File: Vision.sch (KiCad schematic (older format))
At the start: 125 parts, among them J1 Conn_ARM_JTAG_SWD_10, Q1 DTC123J, SW1 SW_Push, U1 MCP1700-3002E_SOT23, U2 STM32F072CBUx, U3 TPD4E05U06DQAR

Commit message: Set switch position
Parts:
- K_,1, K_.1, K_;1, K_A1, K_B1, K_B2, K_C1, K_D1, K_E1, K_F1, K_G1, K_H1, K_I1, K_J1, K_K1, K_L1, K_M1, K_N1, K_O1, K_P1, K_Q1, K_R1, K_S1, K_T1, K_U1, K_V1, K_W1, K_X1, K_Y1, K_Z1: footprint MX_Only:MXOnly-1U-Hotswap-Antishear -> MX_Only:MXOnly-1U-Hotswap
- K_ALT1: value MX-1U -> MX-1.5U; footprint MX_Only:MXOnly-1U-Hotswap-Antishear -> MX_Only:MXOnly-1.5U-Hotswap
- K_ALT2, K_CTRL1, K_CTRL2: value MX-1.25U -> MX-1.5U; footprint MX_Only:MXOnly-1U-Hotswap-Antishear -> MX_Only:MXOnly-1.5U-Hotswap
- K_BSPC1: renamed from K_P2; footprint MX_Only:MXOnly-1U-Hotswap-Antishear -> MX_Only:MXOnly-1U-Hotswap
- K_DEL1, K_ESC1, K_PGUP1: value MX-1.5U -> MX-1U; footprint MX_Only:MXOnly-1U-Hotswap-Antishear -> MX_Only:MXOnly-1U-Hotswap
- K_ENTER1, K_SHIFT1: value MX-2.25U -> MX-1.75U; footprint MX_Only:MXOnly-1U-Hotswap-Antishear -> MX_Only:MXOnly-1.75U-Hotswap
- K_FN1, K_PGDN1: value MX-1.75U -> MX-1U; footprint MX_Only:MXOnly-1U-Hotswap-Antishear -> MX_Only:MXOnly-1U-Hotswap
- K_SHIFT2, K_TAB1: value MX-1.75U -> MX-1.25U; footprint MX_Only:MXOnly-1U-Hotswap-Antishear -> MX_Only:MXOnly-1.25U-Hotswap
- K_SPC1: value MX-1.25U -> MX-2U; footprint MX_Only:MXOnly-1U-Hotswap-Antishear -> MX_Only:MXOnly-2U-Hotswap-ReversedStabilizers
- K_SPC2: value MX-6U -> MX-1.75U; footprint MX_Only:MXOnly-1U-Hotswap-Antishear -> MX_Only:MXOnly-1.75U-Hotswap
- K_WIN1: value MX-2.25U -> MX-1U; footprint MX_Only:MXOnly-1U-Hotswap-Antishear -> MX_Only:MXOnly-1U-Hotswap
- K_WIN2: value MX-2.75U -> MX-1U; footprint MX_Only:MXOnly-1U-Hotswap-Antishear -> MX_Only:MXOnly-1U-Hotswap
- R1, R2, R3, R4, R5, R6: footprint Resistors_SMD:R_0805 -> Resistor_SMD:R_0603_1608Metric
- U2: symbol MCU_ST_STM32F0:STM32F072CBUx -> MCU_ST_STM32F0:STM32F072CBTx
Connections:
- net GND: no longer U2.49 (VSS)

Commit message: Route PCB
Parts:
- added C13: 100nF, Capacitor_SMD:C_0603_1608Metric, symbol Device:C_Small
- added H1: LOGO1, locallib:logo1, symbol Mechanical:MountingHole
- added H2: LOGO2, locallib:logo2, symbol Mechanical:MountingHole
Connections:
- net +3V3: now also C13.1
- net COL0: now also U2.19 (PB1); no longer U2.31 (PA10)
- net COL1: now also U2.18 (PB0); no longer U2.21 (PB10)
- net COL10: now also U2.41 (PB5); no longer U2.11 (PA1)
- net COL11: now also U2.40 (PB4); no longer U2.10 (PA0)
- net COL13: now also U2.38 (PA15); no longer U2.40 (PB4)
- net COL2: now also U2.17 (PA7); no longer U2.20 (PB2)
- net COL3: now also U2.16 (PA6); no longer U2.19 (PB1)
- net COL4: now also U2.15 (PA5); no longer U2.18 (PB0)
- net COL5: now also U2.14 (PA4); no longer U2.17 (PA7)
- net COL6: now also U2.13 (PA3); no longer U2.15 (PA5)
- net COL7: now also U2.45 (PB8); no longer U2.14 (PA4)
- net COL8: now also U2.43 (PB7); no longer U2.13 (PA3)
- net COL9: now also U2.42 (PB6); no longer U2.12 (PA2)
- net GND: now also C13.2
- net ROW0: now also U2.25 (PB12); no longer U2.38 (PA15)
- net ROW1: now also U2.20 (PB2); no longer U2.22 (PB11)
- net ROW2: now also U2.12 (PA2); no longer U2.29 (PA8)
- net ROW3: now also U2.11 (PA1); no longer U2.30 (PA9)
- no-connect marks 11 -> 9
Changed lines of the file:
@@
 Wire Wire Line
 	5300 6200 5300 6350
-Wire Wire Line
-	9300 5750 9400 5750
-Wire Wire Line
-	10275 5750 10275 5525
-Connection ~ 9400 5750
-Wire Wire Line
-	9400 5750 9500 5750
-Connection ~ 9500 5750
-Wire Wire Line
-	9500 5750 9600 5750
-Connection ~ 9600 5750
-Wire Wire Line
-	9600 5750 9700 5750
 $Comp
 L power:+3V3 #PWR02
@@
 Wire Wire Line
 	9050 8750 9050 8900
-Connection ~ 9300 8750
-Wire Wire Line
-	9300 8750 9050 8750
-Connection ~ 9400 8750
-Wire Wire Line
-	9400 8750 9300 8750
-Connection ~ 9500 8750
-Wire Wire Line
-	9500 8750 9400 8750
-Wire Wire Line
-	9600 8750 9500 8750
 $Comp
 L power:GND #PWR013
@@
 Text GLabel 10100 8250 2    50   Input ~ 0
 D+
-Text GLabel 10100 7050 2    50   Input ~ 0
+Text GLabel 8800 7450 0    50   Input ~ 0
 COL11
-Text GLabel 10100 7150 2    50   Input ~ 0
+Text GLabel 8800 7550 0    50   Input ~ 0
 COL10
-Text GLabel 10100 7250 2    50   Input ~ 0
+Text GLabel 8800 7650 0    50   Input ~ 0
 COL9
-Text GLabel 10100 7350 2    50   Input ~ 0
+Text GLabel 8800 7750 0    50   Input ~ 0
 COL8
 NoConn ~ 8800 6750
@@
 NoConn ~ 8800 6450
 NoConn ~ 8800 6650
-NoConn ~ 8800 7650
-NoConn ~ 8800 7750
 Text GLabel 10100 8350 2    50   Input ~ 0
 SWDIO
 Text GLabel 10100 8450 2    50   Input ~ 0
 SWCLK
+Text GLabel 8800 7850 0    50   Input ~ 0
+COL7
+Text GLabel 10100 7350 2    50   Input ~ 0
+COL6
 Text GLabel 10100 7450 2    50   Input ~ 0
-COL7
+COL5
 Text GLabel 10100 7550 2    50   Input ~ 0
-COL6
+COL4
+Text GLabel 10100 7650 2    50   Input ~ 0
+COL3
 Text GLabel 10100 7750 2    50   Input ~ 0
-COL5
+COL2
 Text GLabel 8800 7050 0    50   Input ~ 0
-COL4
+COL1
 Text GLabel 8800 7150 0    50   Input ~ 0
-COL3
+COL0
+Text GLabel 8800 8250 0    50   Input ~ 0
+ROW0
 Text GLabel 8800 7250 0    50   Input ~ 0
-COL2
-Text GLabel 8800 8050 0    50   Input ~ 0
-COL1
-Text GLabel 10100 8050 2    50   Input ~ 0
-COL0
-Text GLabel 10100 8550 2    50   Input ~ 0
-ROW0
-Text GLabel 8800 8150 0    50   Input ~ 0
 ROW1
-Text GLabel 10100 7850 2    50   Input ~ 0
+Text GLabel 10100 7250 2    50   Input ~ 0
 ROW2
-Text GLabel 10100 7950 2    50   Input ~ 0
+Text GLabel 10100 7150 2    50   Input ~ 0
 ROW3
 Text GLabel 8800 6150 0    50   Input ~ 0
@@
 Text GLabel 8800 5950 0    50   Input ~ 0
 NRST
-Connection ~ 9700 5750
-Wire Wire Line
-	9700 5750 10275 5750
-$Comp
-L MCU_ST_STM32F0:STM32F072CBTx U2
-U 1 1 5F7B2EAB
-P 9500 7250
-F 0 "U2" H 9450 8928 50  0000 C CNN
-F 1 "STM32F072CBUx" H 9450 8837 50  0000 C CNN
-F 2 "Package_QFP:LQFP-48_7x7mm_P0.5mm" H 8900 5850 50  0001 R CNN
-F 3 "http://www.st.com/st-web-ui/static/active/en/resource/technical/document/datasheet/DM00090510.pdf" H 9500 7250 50  0001 C CNN
-	1    9500 7250
-	1    0    0    -1
-$EndComp
 $Comp
 L Device:C_Small C12
@@
 Connection ~ 11600 6400
 Wire Wire Line
-	11600 6400 12425 6400
+	11600 6400 11850 6400
 Text GLabel 8800 7350 0    50   Input ~ 0
 COL12
-Text GLabel 8800 7450 0    50   Input ~ 0
+Text GLabel 10100 8550 2    50   Input ~ 0
 COL13
 $Comp
@@
 	1    0    0    -1
 $EndComp
+Wire Wire Line
+	9600 8750 9500 8750
+Connection ~ 9500 8750
+Wire Wire Line
+	9500 8750 9400 8750
+Connection ~ 9400 8750
+Wire Wire Line
+	9400 8750 9300 8750
+Wire Wire Line
+	9300 8750 9050 8750
+Connection ~ 9300 8750
+$Comp
+L MCU_ST_STM32F0:STM32F072CBTx U2
+U 1 1 5F7B2EAB
+P 9500 7250
+F 0 "U2" H 8850 8850 50  0000 C CNN
+F 1 "STM32F072CBUx" H 8850 8750 50  0000 C CNN
+F 2 "Package_QFP:LQFP-48_7x7mm_P0.5mm" H 8900 5850 50  0001 R CNN
+F 3 "http://www.st.com/st-web-ui/static/active/en/resource/technical/document/datasheet/DM00090510.pdf" H 9500 7250 50  0001 C CNN
+	1    9500 7250
+	1    0    0    -1
+$EndComp
+Wire Wire Line
+	9600 5750 9700 5750
+Connection ~ 9600 5750
+Wire Wire Line
+	9500 5750 9600 5750
+Connection ~ 9500 5750
+Wire Wire Line
+	9400 5750 9500 5750
+Connection ~ 9400 5750
+Wire Wire Line
+	9300 5750 9400 5750
+Wire Wire Line
+	10275 5750 10275 5525
+Connection ~ 9700 5750
+Wire Wire Line
+	9700 5750 10275 5750
+$Comp
+L Device:C_Small C13
+U 1 1 5EDDDFE6
+P 11850 6525
+F 0 "C13" H 11860 6595 50  0000 L CNN
+F 1 "100nF" H 11860 6445 50  0000 L CNN
+F 2 "Capacitor_SMD:C_0603_1608Metric" H 11850 6525 50  0001 C CNN
+F 3 "" H 11850 6525 50  0001 C CNN
+	1    11850 6525
+	1    0    0    -1
+$EndComp
+Connection ~ 11850 6400
+Wire Wire Line
+	11850 6400 12425 6400
+Wire Wire Line
+	11850 6400 11850 6425
+Wire Wire Line
+	11600 6650 11850 6650
+Wire Wire Line
+	11850 6650 11850 6625
+Connection ~ 11600 6650
+$Comp
+L Mechanical:MountingHole H1
+U 1 1 5EB4CCDC
+P 10975 2175
+F 0 "H1" H 11075 2221 50  0000 L CNN
+F 1 "LOGO1" H 11075 2130 50  0000 L CNN
+F 2 "locallib:logo1" H 10975 2175 50  0001 C CNN
+F 3 "~" H 10975 2175 50  0001 C CNN
+	1    10975 2175
+	1    0    0    -1
+$EndComp
+$Comp
+L Mechanical:MountingHole H2
+U 1 1 5EB4E9B5
+P 11550 2175
+F 0 "H2" H 11650 2221 50  0000 L CNN
+F 1 "LOGO2" H 11650 2130 50  0000 L CNN
+F 2 "locallib:logo2" H 11550 2175 50  0001 C CNN
+F 3 "~" H 11550 2175 50  0001 C CNN
+	1    11550 2175
+	1    0    0    -1
+$EndComp

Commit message: Add edgerails
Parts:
- added H10, H11, H12, H13, H14, H15, H7, H8, H9: MOUSEBITES, random-keyboard-parts:breakaway-mousebites, symbol Mechanical:MountingHole
- added H3, H4: FIDUCIAL, Fiducial:Fiducial_0.75mm_Mask2.25mm, symbol Mechanical:MountingHole
- added H5, H6: FIDUCIAL, Fiducial:Fiducial_1mm_Mask3mm, symbol Mechanical:MountingHole
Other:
- moved on the sheet: H2
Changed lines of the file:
@@
 L Mechanical:MountingHole H2
 U 1 1 5EB4E9B5
-P 11550 2175
-F 0 "H2" H 11650 2221 50  0000 L CNN
-F 1 "LOGO2" H 11650 2130 50  0000 L CNN
-F 2 "locallib:logo2" H 11550 2175 50  0001 C CNN
-F 3 "~" H 11550 2175 50  0001 C CNN
-	1    11550 2175
+P 11650 2175
+F 0 "H2" H 11750 2221 50  0000 L CNN
+F 1 "LOGO2" H 11750 2130 50  0000 L CNN
+F 2 "locallib:logo2" H 11650 2175 50  0001 C CNN
+F 3 "~" H 11650 2175 50  0001 C CNN
+	1    11650 2175
 	1    0    0    -1
 $EndComp
+$Comp
+L Mechanical:MountingHole H3
+U 1 1 5EB23BAD
+P 10975 2525
+F 0 "H3" H 11075 2571 50  0000 L CNN
+F 1 "FIDUCIAL" H 11075 2480 50  0000 L CNN
+F 2 "Fiducial:Fiducial_0.75mm_Mask2.25mm" H 10975 2525 50  0001 C CNN
+F 3 "~" H 10975 2525 50  0001 C CNN
+	1    10975 2525
+	1    0    0    -1
+$EndComp
+$Comp
+L Mechanical:MountingHole H4
+U 1 1 5EB23BB7
+P 11650 2525
+F 0 "H4" H 11750 2571 50  0000 L CNN
+F 1 "FIDUCIAL" H 11750 2480 50  0000 L CNN
+F 2 "Fiducial:Fiducial_0.75mm_Mask2.25mm" H 11650 2525 50  0001 C CNN
+F 3 "~" H 11650 2525 50  0001 C CNN
+	1    11650 2525
+	1    0    0    -1
+$EndComp
+$Comp
+L Mechanical:MountingHole H5
+U 1 1 5EB31A13
+P 10975 2875
+F 0 "H5" H 11075 2921 50  0000 L CNN
+F 1 "FIDUCIAL" H 11075 2830 50  0000 L CNN
+F 2 "Fiducial:Fiducial_1mm_Mask3mm" H 10975 2875 50  0001 C CNN
+F 3 "~" H 10975 2875 50  0001 C CNN
+	1    10975 2875
+	1    0    0    -1
+$EndComp
+$Comp
+L Mechanical:MountingHole H6
+U 1 1 5EB31A1D
+P 11650 2875
+F 0 "H6" H 11750 2921 50  0000 L CNN
+F 1 "FIDUCIAL" H 11750 2830 50  0000 L CNN
+F 2 "Fiducial:Fiducial_1mm_Mask3mm" H 11650 2875 50  0001 C CNN
+F 3 "~" H 11650 2875 50  0001 C CNN
+	1    11650 2875
+	1    0    0    -1
+$EndComp
+$Comp
+L Mechanical:MountingHole H7
+U 1 1 5EB68B12
+P 10975 3200
+F 0 "H7" H 11075 3246 50  0000 L CNN
+F 1 "MOUSEBITES" H 11075 3155 50  0000 L CNN
+F 2 "random-keyboard-parts:breakaway-mousebites" H 10975 3200 50  0001 C CNN
+F 3 "~" H 10975 3200 50  0001 C CNN
+	1    10975 3200
+	1    0    0    -1
+$EndComp
+$Comp
+L Mechanical:MountingHole H8
+U 1 1 5EB68B1C
+P 11650 3200
+F 0 "H8" H 11750 3246 50  0000 L CNN
+F 1 "MOUSEBITES" H 11750 3155 50  0000 L CNN
+F 2 "random-keyboard-parts:breakaway-mousebites" H 11650 3200 50  0001 C CNN
+F 3 "~" H 11650 3200 50  0001 C CNN
+	1    11650 3200
+	1    0    0    -1
+$EndComp
+$Comp
+L Mechanical:MountingHole H10
+U 1 1 5EB8518B
+P 11650 3500
+F 0 "H10" H 11750 3546 50  0000 L CNN
+F 1 "MOUSEBITES" H 11750 3455 50  0000 L CNN
+F 2 "random-keyboard-parts:breakaway-mousebites" H 11650 3500 50  0001 C CNN
+F 3 "~" H 11650 3500 50  0001 C CNN
+	1    11650 3500
+	1    0    0    -1
+$EndComp
+$Comp
+L Mechanical:MountingHole H9
+U 1 1 5EB85181
+P 10975 3500
+F 0 "H9" H 11075 3546 50  0000 L CNN
+F 1 "MOUSEBITES" H 11075 3455 50  0000 L CNN
+F 2 "random-keyboard-parts:breakaway-mousebites" H 10975 3500 50  0001 C CNN
+F 3 "~" H 10975 3500 50  0001 C CNN
+	1    10975 3500
+	1    0    0    -1
+$EndComp
+$Comp
+L Mechanical:MountingHole H11
+U 1 1 5EB9F0B1
+P 10975 3800
+F 0 "H11" H 11075 3846 50  0000 L CNN
+F 1 "MOUSEBITES" H 11075 3755 50  0000 L CNN
+F 2 "random-keyboard-parts:breakaway-mousebites" H 10975 3800 50  0001 C CNN
+F 3 "~" H 10975 3800 50  0001 C CNN
+	1    10975 3800
+	1    0    0    -1
+$EndComp
+$Comp
+L Mechanical:MountingHole H12
+U 1 1 5EB9F0BB
+P 11650 3800
+F 0 "H12" H 11750 3846 50  0000 L CNN
+F 1 "MOUSEBITES" H 11750 3755 50  0000 L CNN
+F 2 "random-keyboard-parts:breakaway-mousebites" H 11650 3800 50  0001 C CNN
+F 3 "~" H 11650 3800 50  0001 C CNN
+	1    11650 3800
+	1    0    0    -1
+$EndComp
+$Comp
+L Mechanical:MountingHole H14
+U 1 1 5EB9F0C5
+P 11650 4100
+F 0 "H14" H 11750 4146 50  0000 L CNN
+F 1 "MOUSEBITES" H 11750 4055 50  0000 L CNN
+F 2 "random-keyboard-parts:breakaway-mousebites" H 11650 4100 50  0001 C CNN
+F 3 "~" H 11650 4100 50  0001 C CNN
+	1    11650 4100
+	1    0    0    -1
+$EndComp
+$Comp
+L Mechanical:MountingHole H13
+U 1 1 5EB9F0CF
+P 10975 4100
+F 0 "H13" H 11075 4146 50  0000 L CNN
+F 1 "MOUSEBITES" H 11075 4055 50  0000 L CNN
+F 2 "random-keyboard-parts:breakaway-mousebites" H 10975 4100 50  0001 C CNN
+F 3 "~" H 10975 4100 50  0001 C CNN
+	1    10975 4100
+	1    0    0    -1
+$EndComp
+$Comp
+L Mechanical:MountingHole H15
+U 1 1 5EBACADD
+P 10975 4400
+F 0 "H15" H 11075 4446 50  0000 L CNN
+F 1 "MOUSEBITES" H 11075 4355 50  0000 L CNN
+F 2 "random-keyboard-parts:breakaway-mousebites" H 10975 4400 50  0001 C CNN
+F 3 "~" H 10975 4400 50  0001 C CNN
+	1    10975 4400
+	1    0    0    -1
+$EndComp

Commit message: Add BOM
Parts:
- D1, D10, D11, D12, D13, D14, D15, D16, D17, D18, D19, D2, D20, D21, D22, D23, D24, D25, D26, D27, D28, D29, D3, D30, D31, D32, D33, D34, D35, D36, D37, D38, D39, D4, D40, D41, D42, D43, D44, D45, D46, D47, D48, D5, D6, D7, D8, D9: value SOD-123 -> 1N4148W
- Q1: footprint Package_TO_SOT_SMD:SC-59 -> Package_TO_SOT_SMD:SOT-23
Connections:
- no-connect marks 9 -> 19

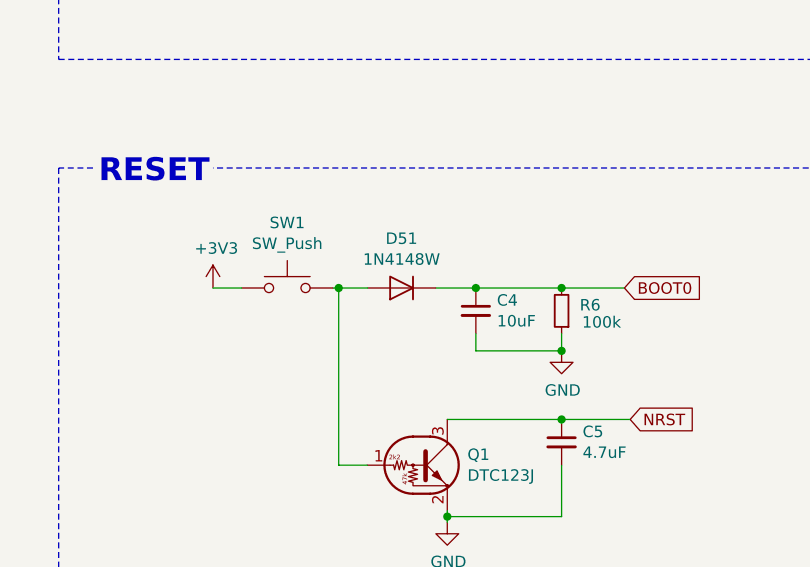
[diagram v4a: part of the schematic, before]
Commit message: Add files for Elecrow PCBA
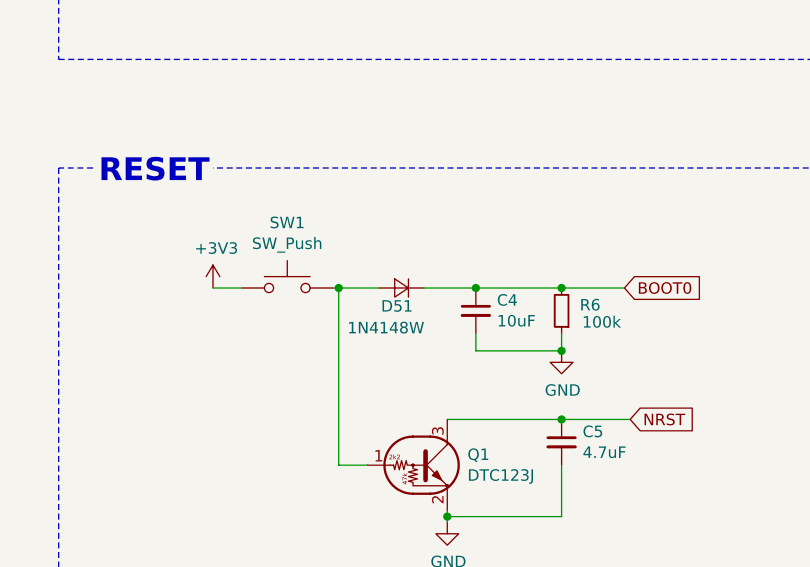
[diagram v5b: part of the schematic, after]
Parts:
- removed D51: 1N4148W, Diode_SMD:D_SOD-123, symbol Diode:1N4148
- added D51: 1N4148W, Diode_SMD:D_SOD-123, symbol Device:D_Small
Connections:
- net BOOT0: now also D51.1 (K)
- net at Q1.1 (B), SW1.2: now also D51.2 (A)
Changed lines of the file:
@@
-$EndComp
-$Comp
-L Device:D_Small D44
-U 1 1 5D653AA5
-P 5375 4225
-F 0 "D44" H 5325 4305 50  0000 L CNN
-F 1 "1N4148W" H 5275 4400 50  0000 L CNN
-F 2 "Diode_SMD:D_SOD-123" V 5375 4225 50  0001 C CNN
-F 3 "" V 5375 4225 50  0001 C CNN
-	1    5375 4225
-	0    -1   -1   0
 $EndComp
 $Comp
@@
 	3575 4325 4775 4325
 Connection ~ 4775 4325
-Wire Wire Line
-	4775 4325 5375 4325
-Connection ~ 5375 4325
-Wire Wire Line
-	5375 4325 5975 4325
 Connection ~ 5975 4325
 Wire Wire Line
@@
 Text Notes 4125 7875 0    100  ~ 20
 RESET
-$Comp
-L Diode:1N4148 D51
-U 1 1 5F9245F3
-P 5450 8325
-F 0 "D51" H 5450 8109 50  0000 C CNN
-F 1 "1N4148W" H 5450 8200 50  0000 C CNN
-F 2 "Diode_SMD:D_SOD-123" H 5450 8150 50  0001 C CNN
-F 3 "https://assets.nexperia.com/documents/data-sheet/1N4148_1N4448.pdf" H 5450 8325 50  0001 C CNN
-	1    5450 8325
-	-1   0    0    1
-$EndComp
 Wire Wire Line
 	5150 8325 5175 8325
@@
 	-1   0    0    1
 $EndComp
-Wire Wire Line
-	5600 8325 5775 8325
 Connection ~ 5775 8325
 Wire Wire Line
@@
 	5175 9100 5300 9100
 Connection ~ 5175 8325
-Wire Wire Line
-	5175 8325 5300 8325
 Wire Notes Line
 	4100 7800 3950 7800
@@
 NoConn ~ 8800 8450
 NoConn ~ 8800 8550
+Connection ~ 5375 4325
+Wire Wire Line
+	5375 4325 5975 4325
+Wire Wire Line
+	4775 4325 5375 4325
+$Comp
+L Device:D_Small D44
+U 1 1 5D653AA5
+P 5375 4225
+F 0 "D44" H 5325 4305 50  0000 L CNN
+F 1 "1N4148W" H 5275 4400 50  0000 L CNN
+F 2 "Diode_SMD:D_SOD-123" V 5375 4225 50  0001 C CNN
+F 3 "" V 5375 4225 50  0001 C CNN
+	1    5375 4225
+	0    -1   -1   0
+$EndComp
+$Comp
+L Device:D_Small D51
+U 1 1 5EF0D724
+P 5450 8325
+F 0 "D51" H 5400 8405 50  0000 L CNN
+F 1 "1N4148W" H 5350 8500 50  0000 L CNN
+F 2 "Diode_SMD:D_SOD-123" V 5450 8325 50  0001 C CNN
+F 3 "" V 5450 8325 50  0001 C CNN
+	1    5450 8325
+	-1   0    0    1
+$EndComp
+Wire Wire Line
+	5550 8325 5775 8325
+Wire Wire Line
+	5175 8325 5350 8325
 $EndSCHEMATC

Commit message: Update schematics
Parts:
- added K_SHIFT3: MX-1.25U, MX_Only:MXOnly-2.25U-NoLED, symbol MX_Alps_Hybrid:MX-NoLED
- added K_SPC3: MX-2U, MX_Only:MXOnly-1.75U-NoLED, symbol MX_Alps_Hybrid:MX-NoLED
- added K_SPC4: MX-1.75U, MX_Only:MXOnly-1U-NoLED, symbol MX_Alps_Hybrid:MX-NoLED
- added K_WIN3: MX-1U, MX_Only:MXOnly-1.25U-NoLED, symbol MX_Alps_Hybrid:MX-NoLED
- added K_WIN4: MX-1U, MX_Only:MXOnly-1.75U-NoLED, symbol MX_Alps_Hybrid:MX-NoLED
- K_,1, K_.1, K_;1, K_A1, K_B1, K_B2, K_BSPC1, K_C1, K_D1, K_DEL1, K_E1, K_ESC1, K_F1, K_FN1, K_G1, K_H1, K_I1, K_J1, K_K1, K_L1, K_M1, K_N1, K_O1, K_P1, K_PGDN1, K_PGUP1, K_Q1, K_R1, K_S1, K_T1, K_U1, K_V1, K_W1, K_WIN1, K_WIN2, K_X1, K_Y1, K_Z1: footprint MX_Only:MXOnly-1U-Hotswap -> MX_Only:MXOnly-1U-NoLED
- K_ALT1, K_ALT2, K_CTRL1, K_CTRL2: footprint MX_Only:MXOnly-1.5U-Hotswap -> MX_Only:MXOnly-1.5U-NoLED
- K_ENTER1, K_SHIFT1: footprint MX_Only:MXOnly-1.75U-Hotswap -> MX_Only:MXOnly-1.75U-NoLED
- K_SHIFT2, K_TAB1: footprint MX_Only:MXOnly-1.25U-Hotswap -> MX_Only:MXOnly-1.25U-NoLED
- K_SPC1: footprint MX_Only:MXOnly-2U-Hotswap-ReversedStabilizers -> MX_Only:MXOnly-2U-ReversedStabilizers-NoLED
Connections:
- net COL12: now also K_SHIFT3.1 (COL)
- net COL5: now also K_SPC3.1 (COL)
- net COL6: now also K_WIN3.1 (COL)
- net COL7: now also K_SPC4.1 (COL)
- net COL9: now also K_WIN4.1 (COL)
- net at D39.2 (A), K_SHIFT2.2 (ROW): now also K_SHIFT3.2 (ROW)
- net at D45.2 (A), K_SPC2.2 (ROW): now also K_SPC4.2 (ROW)
- net at D43.2 (A), K_SPC1.2 (ROW): now also K_SPC3.2 (ROW)
- net at D44.2 (A), K_WIN1.2 (ROW): now also K_WIN3.2 (ROW)
- net at D46.2 (A), K_WIN2.2 (ROW): now also K_WIN4.2 (ROW)
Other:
- moved on the sheet: C1, C10, C11, C12, C13, C2, C3, C4, C5, C6, C7, C8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

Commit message: Update PCB
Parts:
- K_SPC2: footprint MX_Only:MXOnly-1.75U-Hotswap -> MX_Only:MXOnly-1.75U-NoLED
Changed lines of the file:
@@
 F 0 "K_SPC2" H 6025 4125 60  0000 C CNN
 F 1 "MX-1.75U" H 6025 4025 20  0000 C CNN
-F 2 "MX_Only:MXOnly-1.75U-Hotswap" H 6000 3950 60  0001 C CNN
+F 2 "MX_Only:MXOnly-1.75U-NoLED" H 6000 3950 60  0001 C CNN
 F 3 "" H 6000 3950 60  0001 C CNN
 	1    6025 3975
